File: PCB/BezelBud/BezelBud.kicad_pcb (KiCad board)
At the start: 4 copper layers, 64 parts, among them J1 USB_C_Receptacle_USB2.0_16P, J2 Conn_01x05_Pin, SW1 SW_SPDT, SW2 SW_SPDT, SW3 SW_SPDT, SW4 SW_SPDT, SW5 SW_SPDT, SW6 SW_SPDT, SW7 SW_SPDT, SW8 SW_SPDT, SW9 SW_SPDT, U1 STM32F072CBT6, U2 USBLC6-2SC6, U3 LP5907MFX-3.3, U4 LP5907MFX-3.3, U5 PCM1861DBT, Y1 Crystal_GND24

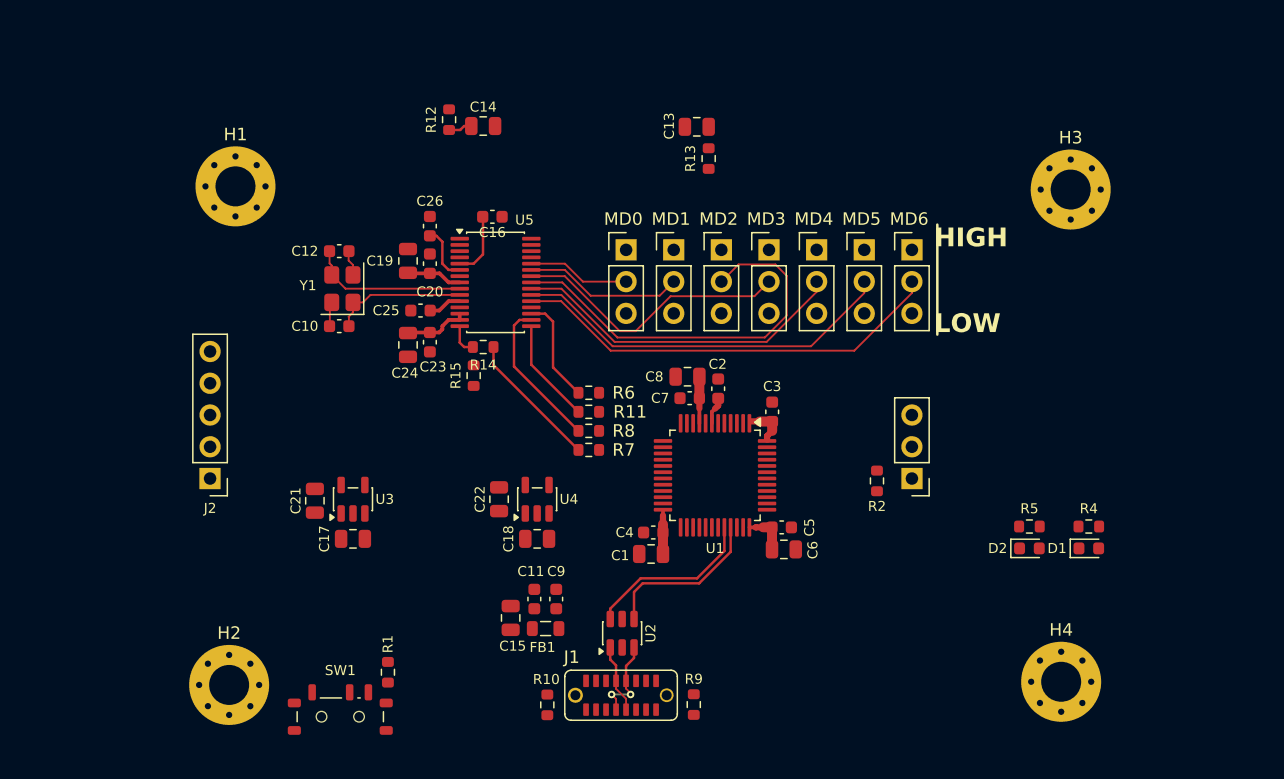
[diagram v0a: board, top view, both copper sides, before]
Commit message: small updates to schematic and layout for new stm32
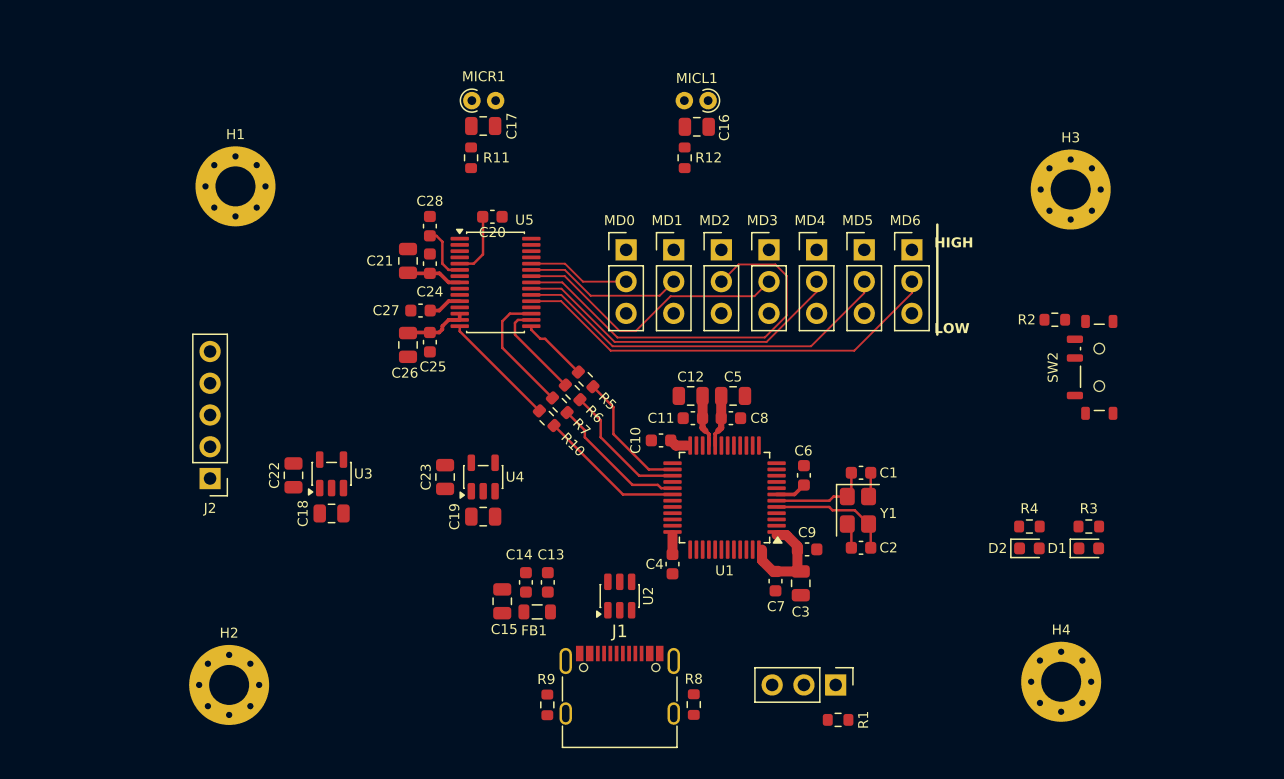
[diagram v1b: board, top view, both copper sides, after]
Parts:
- removed the C6 at (155.9, 82.1)
- removed R14, R15: 0R, Resistor_SMD:R_0603_1608Metric
- added C11: 0.1uF, Capacitor_SMD:C_0603_1608Metric, F.Cu at (148.6, 71.6)
- added C12: 1uF, Capacitor_SMD:C_0805_2012Metric, F.Cu at (148.4, 69.8)
- added C4: 0.1uF, Capacitor_SMD:C_0603_1608Metric, F.Cu at (147.0, 83.3)
- added MICL1: Microphone_Condenser, Resistor_THT:R_Axial_DIN0204_L3.6mm_D1.6mm_P1.90mm_Vertical, F.Cu at (149.8, 46.2)
- added MICR1: Microphone_Condenser, Resistor_THT:R_Axial_DIN0204_L3.6mm_D1.6mm_P1.90mm_Vertical, F.Cu at (130.9, 46.2)
- C5: value 0.1uF -> 1uF; footprint Capacitor_SMD:C_0603_1608Metric -> Capacitor_SMD:C_0805_2012Metric
- C7: value 10nF -> 0.1uF
- C8: value 1uF -> 10nF; footprint Capacitor_SMD:C_0805_2012Metric -> Capacitor_SMD:C_0603_1608Metric
- J1: footprint BezelBud:CONN RCPT Type-C 16POS SMD TC-005 -> Connector_USB:USB_C_Receptacle_G-Switch_GT-USB-7010ASV
- R3: renamed from R4; value 220 -> 1K
- R4: renamed from R5; value 220 -> 1K
- U1: value STM32F072CBT6 -> STM32G431CBT6
- moved SW2 66.8 mm to (181.1, 67.6), turned to 90 degrees
- moved R2 60.3 mm to (177.5, 63.8), turned to 0 degrees
- moved C2 48.0 mm to (162.0, 82.0), turned to 180 degrees
- moved Y1 44.9 mm to (161.8, 79.0), turned to -90 degrees
- moved C1 43.4 mm to (162.0, 76.0), turned to 0 degrees
- moved R1 19.4 mm to (160.2, 95.8), turned to 180 degrees
- moved SW1 17.6 mm to (160.0, 93.0), turned to -90 degrees
- moved C7 16.2 mm to (155.2, 84.7), turned to -90 degrees
- moved C3 12.2 mm to (157.2, 84.8), turned to -90 degrees
- moved C9 11.4 mm to (157.7, 82.1), turned to 0 degrees
- moved C5 11.2 mm to (151.8, 69.8)
- moved C6 9.75 mm to (157.5, 76.2)
- moved C10 7.39 mm to (146.1, 73.4)
- moved C8 4.80 mm to (151.6, 71.6), turned to 0 degrees
- moved C19 4.67 mm to (131.8, 79.5)
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- renumbered C10 to C1, C4 to C10, C9 to C13, C11 to C14, C13 to C16, C14 to C17, C17 to C18, C18 to C19, C12 to C2, C16 to C20, C19 to C21, C21 to C22, C22 to C23, C20 to C24, C23 to C25, C24 to C26, C25 to C27, C26 to C28, C1 to C3, C2 to C6, C3 to C9, R2 to R1, R7 to R10, R12 to R11, R13 to R12, R1 to R2, R11 to R5, R8 to R6, R6 to R7, R9 to R8, R10 to R9, SW2 to SW1, SW1 to SW2
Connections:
- C7 pad 1: +3.3VA -> +3.3V
- R10 pad 1: /I2S1_MCK -> /I2S2_MCK
- R10 pad 2: /I2S1_MCK_ST -> /I2S2_MCK_ST
- R5 pad 1: /I2S1_WS -> /I2S2_WS_ST
- R5 pad 2: /I2S1_WS_ST -> /I2S2_WS
- R6 pad 1: /I2S1_CK -> /I2S2_CK_ST
- R6 pad 2: /I2S1_CK_ST -> /I2S2_CK
- R7 pad 1: /I2S1_SD -> /I2S2_SD_ST
- R7 pad 2: /I2S1_SD_ST -> /I2S2_SD
- U1 pad 14: /I2S1_WS_ST -> unconnected-(U1-PA6-Pad14)
- U1 pad 15: /I2S1_CK_ST -> unconnected-(U1-PA7-Pad15)
- U1 pad 16: /I2S1_MCK_ST -> /LED_BLINK
- U1 pad 17: /I2S1_SD_ST -> /LED_LIVE
- U1 pad 18: unconnected-(U1-PB0-Pad18) -> /MUTE_SW
- U1 pad 19: unconnected-(U1-PB1-Pad19) -> GND
- U1 pad 20: unconnected-(U1-PB2-Pad20) -> +3.3VA
- U1 pad 21: unconnected-(U1-PB10-Pad21) -> +3.3VA
- U1 pad 26: /LED_BLINK -> /I2S2_WS_ST
- U1 pad 27: /LED_LIVE -> /I2S2_CK_ST
- U1 pad 28: /MUTE_SW -> unconnected-(U1-PB14-Pad28)
- U1 pad 29: unconnected-(U1-PA8-Pad29) -> /I2S2_SD_ST
- U1 pad 30: /INT -> /I2S2_MCK_ST
- U1 pad 31: unconnected-(U1-PA10-Pad31) -> /INT
- U1 pad 32: /USB_N -> unconnected-(U1-PA10-Pad32)
- U1 pad 33: /USB_P -> /USB_N
- U1 pad 34: /SWDIO -> /USB_P
- U1 pad 36: +3.3VA -> +3.3V
- U1 pad 37: /SWLCK -> /SWDIO
- U1 pad 38: unconnected-(U1-PA15-Pad38) -> /SWLCK
- U1 pad 44: /BOOT0 -> unconnected-(U1-PB7-Pad44)
- U1 pad 45: unconnected-(U1-PB8-Pad45) -> /BOOT0
- U1 pad 5: unconnected-(U1-PF0-Pad5) -> /PF0
- U1 pad 6: unconnected-(U1-PF1-Pad6) -> /PF1
- U1 pad 8: GND -> unconnected-(U1-PA0-Pad8)
- U1 pad 9: +3.3VA -> unconnected-(U1-PA1-Pad9)
- U5 pad 10: /PF1 -> unconnected-(U5-XI-Pad10)
- U5 pad 15: /SCKI -> /I2S2_MCK
- U5 pad 16: /I2S1_WS -> /I2S2_WS
- U5 pad 17: /I2S1_CK -> /I2S2_CK
- U5 pad 18: /I2S1_SD -> /I2S2_SD
- U5 pad 9: /PF0 -> unconnected-(U5-XO-Pad9)
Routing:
- net /USB_N: track 13.8 -> 0.00 mm
- net /USB_P: track 13.2 -> 0.00 mm
- net /I2S1_CK: track 12.1 -> 0.00 mm
- net /I2S2_MCK_ST: track 0.00 -> 11.8 mm
- net /I2S2_SD_ST: track 0.00 -> 11.3 mm
- net /I2S1_MCK: track 11.0 -> 0.00 mm
- net /I2S2_CK_ST: track 0.00 -> 10.7 mm
- net /I2S2_WS_ST: track 0.00 -> 10.4 mm
- net /I2S2_SD: track 0.00 -> 10.4 mm
- net /I2S2_MCK: track 0.00 -> 9.42 mm
- net /I2S1_SD: track 8.54 -> 0.00 mm
- net /I2S1_WS: track 8.41 -> 0.00 mm
- net /I2S2_CK: track 0.00 -> 8.05 mm
- net /USBC_P: track 6.95 -> 0.00 mm, vias 2 -> 0
- net /USBC_N: track 5.50 -> 0.00 mm
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
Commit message: updated pcb layout
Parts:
- added C18: 47uF, Capacitor_SMD:C_1206_3216Metric, F.Cu at (171.7, 92.3)
- added C20: 47uF, Capacitor_SMD:C_1206_3216Metric, F.Cu at (169.4, 92.3)
- added R13: 100R, Resistor_SMD:R_0805_2012Metric, F.Cu at (166.6, 91.0)
- moved J2 60.0 mm to (169.9, 75.2), turned to 0 degrees
- moved C26 47.7 mm to (176.3, 71.5), turned to 0 degrees
- moved C24 47.1 mm to (162.3, 87.6)
- moved H4 46.9 mm to (169.4, 46.6)
- moved H2 45.2 mm to (98.4, 49.7)
- moved C23 44.5 mm to (176.3, 78.0)
- moved U4 44.5 mm to (176.3, 74.8)
- moved SW3 44.0 mm to (112.0, 84.8)
- moved SW4 44.0 mm to (115.8, 84.8)
- moved SW5 44.0 mm to (127.3, 84.8)
- moved SW6 44.0 mm to (108.2, 84.8)
- moved SW7 44.0 mm to (119.6, 84.8)
- moved SW8 44.0 mm to (123.4, 84.8)
- moved SW9 44.0 mm to (131.1, 84.8)
- moved U3 40.9 mm to (158.9, 87.6), turned to 0 degrees
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- renumbered C18 to C19, C20 to C21, C21 to C22, C19 to C23, C22 to C24, C24 to C25, C23 to C26, C25 to C27, C26 to C28, C27 to C29, C28 to C30
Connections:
- C23 pad 1: +5V -> +5VFIL
- U4 pad 1: +5V -> +5VFIL
- U4 pad 3: +5V -> +5VFIL
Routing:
- net /MD6: track 34.9 -> 0.00 mm
- net /MD2: track 32.3 -> 0.00 mm
- net /MD5: track 31.0 -> 0.00 mm
- net /MD4: track 27.1 -> 0.00 mm
- net /MD3: track 22.5 -> 0.00 mm
- net /USB_N: track 0.00 -> 12.8 mm
- net /USB_P: track 0.00 -> 12.8 mm
- net /MD1: track 12.7 -> 0.00 mm
- net /I2S2_MCK_ST: track 11.8 -> 0.00 mm
- net /I2S2_SD_ST: track 11.3 -> 0.00 mm
- net /I2S2_CK_ST: track 10.7 -> 0.00 mm
- net /I2S2_WS_ST: track 10.4 -> 0.00 mm
- net /I2S2_MCK: track 9.42 -> 0.00 mm
- net /MD0: track 8.18 -> 0.00 mm
- net /VREF: track 4.54 -> 0.00 mm
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- removed copper zone on In1.Cu, net GND

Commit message: Updated PCB
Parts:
- added C31: 0.1uF, Capacitor_SMD:C_0603_1608Metric, F.Cu at (133.9, 94.2)
- added R14: 1M, Resistor_SMD:R_0603_1608Metric, F.Cu at (135.4, 94.3)
- moved H3 80.3 mm to (112.5, 93.2)
- moved H2 75.0 mm to (172.0, 64.0)
- moved SW2 65.1 mm to (125.5, 96.0), turned to 0 degrees
- moved R2 46.9 mm to (138.8, 84.8), turned to -90 degrees
- moved H4 46.7 mm to (172.0, 93.2)
- moved SW1 33.0 mm to (147.0, 84.9), turned to 90 degrees
- moved R4 28.2 mm to (159.8, 91.0)
- moved D2 28.1 mm to (159.8, 92.8)
- moved R3 28.0 mm to (164.7, 91.0)
- moved D1 27.9 mm to (164.8, 92.8)
- moved R1 25.3 mm to (154.5, 82.2), turned to 180 degrees
- moved H1 16.3 mm to (112.5, 64.0)
- moved R12 14.7 mm to (125.2, 64.4), turned to -90 degrees
- moved R8 12.4 mm to (148.8, 94.2)
- moved C18 10.1 mm to (173.2, 82.3), turned to 0 degrees
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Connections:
- net Net-(D1-A) renamed /R_A
- net Net-(D2-A) renamed /G_A
- J1 pad S1: GND -> /SHIELD
- U1 pad 16: /LED_BLINK -> unconnected-(U1-PB0-Pad16)
- U1 pad 17: /LED_LIVE -> unconnected-(U1-PB1-Pad17)
- U1 pad 18: /MUTE_SW -> unconnected-(U1-PB2-Pad18)
- U1 pad 41: unconnected-(U1-PB4-Pad41) -> /LED_BLINK
- U1 pad 42: unconnected-(U1-PB5-Pad42) -> /LED_LIVE
- U1 pad 43: unconnected-(U1-PB6-Pad43) -> /MUTE_SW
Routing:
- net +3.3VA: track 12.5 -> 93.0 mm
- net +3.3V: track 16.6 -> 73.6 mm, vias 0 -> 8
- net GND: track 4.01 -> 54.7 mm, vias 0 -> 199
- net /MUTE_SW: track 0.00 -> 37.6 mm, vias 0 -> 2
- net +5V: track 0.00 -> 34.7 mm
- net /LED_LIVE: track 0.00 -> 29.9 mm, vias 0 -> 2
- net /LED_BLINK: track 0.00 -> 29.0 mm, vias 0 -> 2
- net /MD0: track 0.00 -> 27.1 mm, vias 0 -> 1
- net /SWDIO: track 0.00 -> 24.9 mm, vias 0 -> 2
- net VCC: track 0.00 -> 24.1 mm
- net /SWLCK: track 0.00 -> 23.5 mm, vias 0 -> 2
- net /MD1: track 0.00 -> 22.9 mm, vias 0 -> 1
- net /SHIELD: track 0.00 -> 22.9 mm, vias 0 -> 1
- net /MD2: track 0.00 -> 22.8 mm, vias 0 -> 1
- net /INT: track 0.00 -> 20.3 mm, vias 0 -> 2
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- added copper zone on B.Cu, net +3.3V
- added copper zone on F.Cu, net +3.3V
- added copper zone on F.Cu, net GND
- added copper zone on In1.Cu, net GND
- added copper zone on In2.Cu, net GND
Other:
- board outline added: 70.1 x 39.6 mm
- board text added: "BEVEL"
- board text added: "BLINK"
- board text added: "DEBUG"
- board text added: "MUTE"
- board text added: "PRG"
- board text added: "RUN"
- board text added: "V1.0 - 02/14/2026"

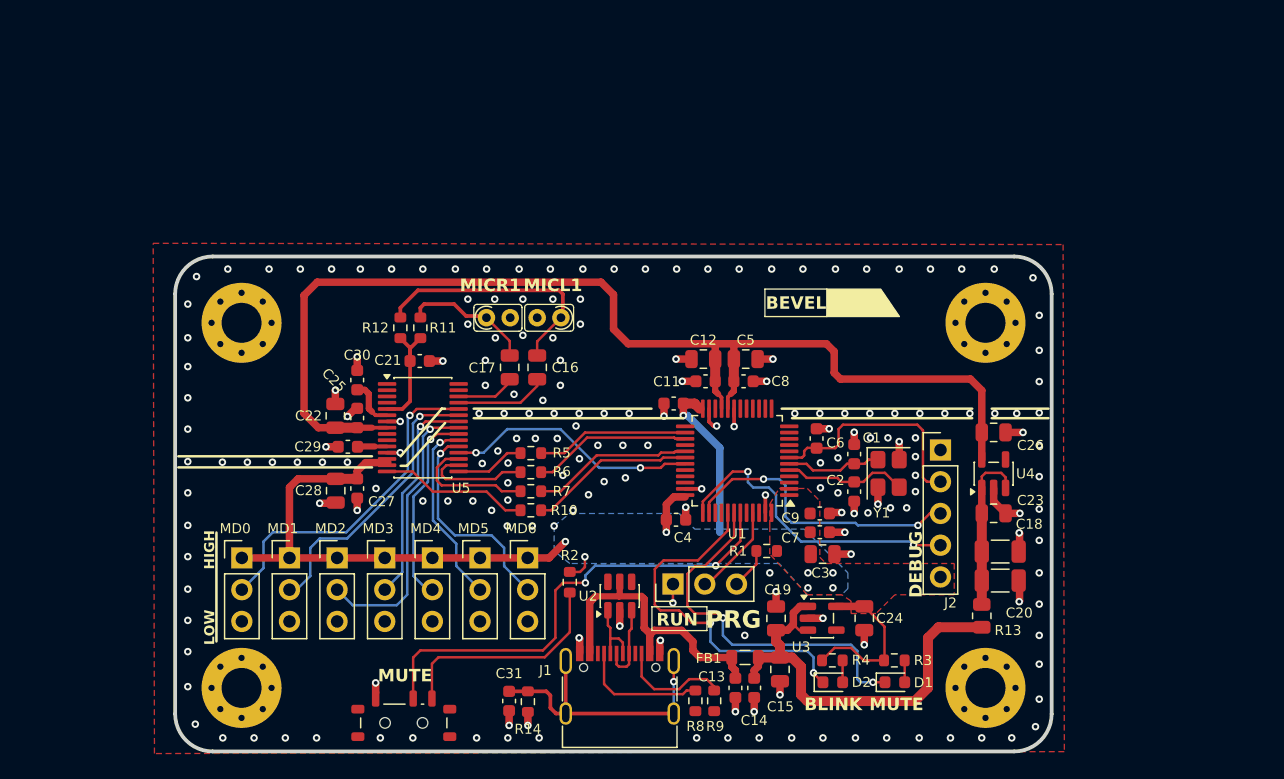
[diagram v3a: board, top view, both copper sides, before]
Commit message: Added bleed resistor and cap to shield <> GND con
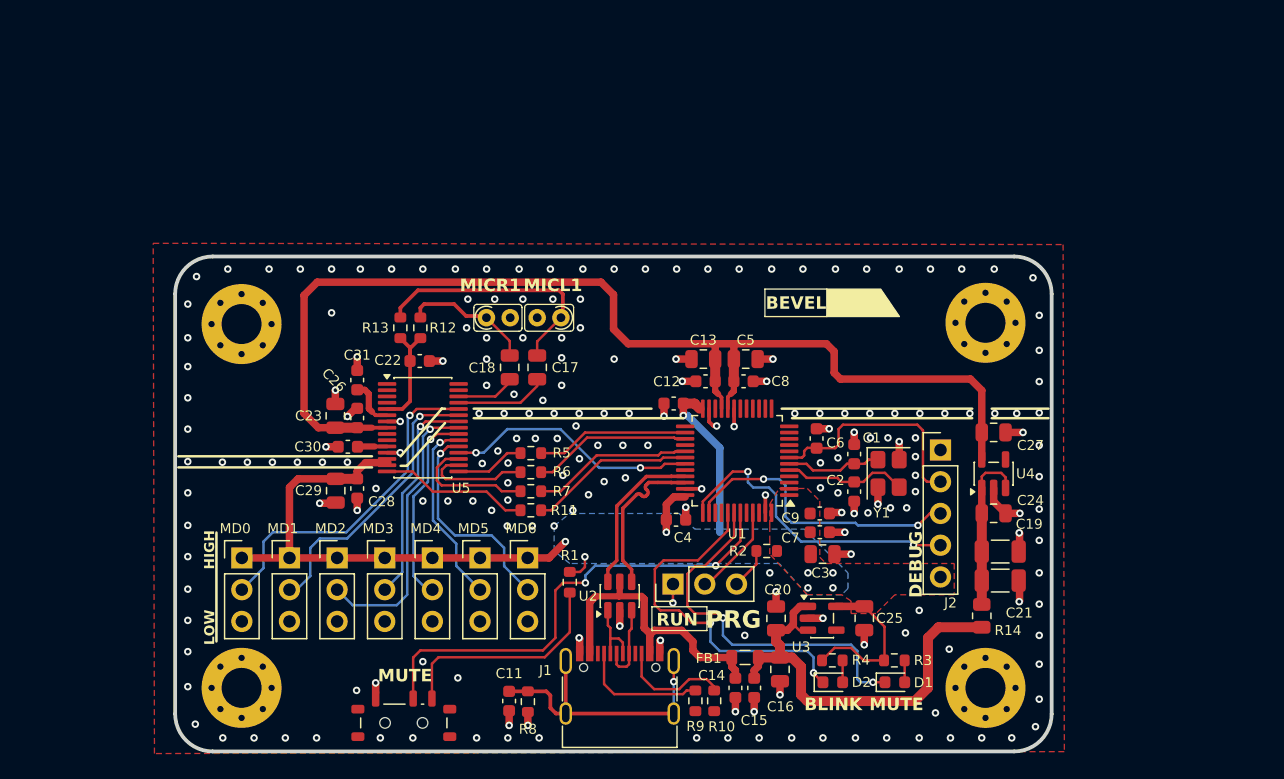
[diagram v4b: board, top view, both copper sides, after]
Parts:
- H1, H2, H3, H4: value MountingHole -> MountingHole_Pad
- moved H1 0.10 mm to (112.5, 64.1)
- renumbered C31 to C11, C11 to C12, C12 to C13, C13 to C14, C14 to C15, C15 to C16, C16 to C17, C17 to C18, C18 to C19, C19 to C20, C20 to C21, C21 to C22, C22 to C23, C23 to C24, C24 to C25, C25 to C26, C26 to C27, C27 to C28, C28 to C29, C29 to C30, C30 to C31, R2 to R1, R9 to R10, R10 to R11, R11 to R12, R12 to R13, R13 to R14, R1 to R2, R14 to R8, R8 to R9, SW2 to SW1, SW1 to SW2
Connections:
- net /INT renamed INT
- net /PF0 renamed PF0
- net /PF1 renamed PF1
- H1 pad 1: (no net) -> GND
- H2 pad 1: (no net) -> GND
- H3 pad 1: (no net) -> GND
- H4 pad 1: (no net) -> GND
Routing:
- net /USB_N: track 0.00 -> 12.8 mm
- net /USB_P: track 0.00 -> 12.8 mm
- net GND: vias 199 -> 208

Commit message: updated layout picture
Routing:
- net /USBC_P: track 6.42 -> 7.07 mm
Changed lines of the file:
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@@
-	)
-	(segment
-		(start 141.996 89.25)
-		(end 141.996 90.45)
-		(width 0.2)
-		(layer "F.Cu")
-		(net 22)
-	)
-	(segment
-		(start 141.996 88.402)
-		(end 141.996 89.25)
-		(width 0.2)
-		(layer "F.Cu")
-		(net 22)
-	)
-	(segment
-		(start 141.798 86.9895)
-		(end 141.798 88.204)
-		(width 0.2)
-		(layer "F.Cu")
-		(net 22)
-	)
-	(segment
-		(start 142.668 89.25)
-		(end 141.996 89.25)
-		(width 0.2)
-		(layer "F.Cu")
-		(net 22)
-	)
-	(segment
-		(start 141.798 88.204)
-		(end 141.996 88.402)
-		(width 0.2)
-		(layer "F.Cu")
-		(net 22)
 	)
 	(segment
 		(start 142.996 90.45)
-		(end 142.996 89.578)
-		(width 0.2)
-		(layer "F.Cu")
-		(net 22)
-	)
-	(segment
-		(start 142.996 89.578)
-		(end 142.668 89.25)
-		(width 0.2)
+		(end 143.006 90.44)
+		(width 0.28)
+		(layer "F.Cu")
+		(net 22)
+	)
+	(segment
+		(start 142.8 89.3)
+		(end 141.996 89.3)
+		(width 0.28)
+		(layer "F.Cu")
+		(net 22)
+	)
+	(segment
+		(start 141.996 88.704)
+		(end 142 88.7)
+		(width 0.3)
+		(layer "F.Cu")
+		(net 22)
+	)
+	(segment
+		(start 141.996 89.3)
+		(end 141.996 88.704)
+		(width 0.3)
+		(layer "F.Cu")
+		(net 22)
+	)
+	(segment
+		(start 142.996 89.496)
+		(end 142.8 89.3)
+		(width 0.28)
+		(layer "F.Cu")
+		(net 22)
+	)
+	(segment
+		(start 142.996 90.45)
+		(end 142.996 89.496)
+		(width 0.28)
+		(layer "F.Cu")
+		(net 22)
+	)
+	(segment
+		(start 141.996 90.45)
+		(end 141.996 89.3)
+		(width 0.3)
+		(layer "F.Cu")
+		(net 22)
+	)
+	(segment
+		(start 141.798 88.498)
+		(end 141.798 86.9895)
+		(width 0.3)
+		(layer "F.Cu")
+		(net 22)
+	)
+	(segment
+		(start 142 88.7)
+		(end 141.798 88.498)
+		(width 0.3)
+		(layer "F.Cu")
+		(net 22)
+	)
+	(segment
+		(start 143.006 90.44)
+		(end 143.006 90.277508)
+		(width 0.28)
 		(layer "F.Cu")
 		(net 22)
@@
 	)
 	(segment
+		(start 143.698 88.502)
+		(end 143.698 86.9895)
+		(width 0.28)
+		(layer "F.Cu")
+		(net 25)
+	)
+	(segment
+		(start 143.496 88.704)
+		(end 143.698 88.502)
+		(width 0.28)
+		(layer "F.Cu")
+		(net 25)
+	)
+	(segment
+		(start 143.496 91.504)
+		(end 143.496 90.45)
+		(width 0.3)
+		(layer "F.Cu")
+		(net 25)
+	)
+	(segment
 		(start 143.496 90.45)
-		(end 143.496 91.301241)
-		(width 0.2)
-		(layer "F.Cu")
-		(net 25)
-	)
-	(segment
-		(start 142.496 91.322)
-		(end 142.496 90.45)
-		(width 0.2)
-		(layer "F.Cu")
-		(net 25)
-	)
-	(segment
-		(start 143.698 88.458)
-		(end 143.698 86.9895)
-		(width 0.2)
-		(layer "F.Cu")
-		(net 25)
-	)
-	(segment
-		(start 143.297241 91.5)
-		(end 142.674 91.5)
-		(width 0.2)
-		(layer "F.Cu")
-		(net 25)
-	)
-	(segment
-		(start 142.674 91.5)
-		(end 142.496 91.322)
-		(width 0.2)
+		(end 143.496 88.704)
+		(width 0.28)
+		(layer "F.Cu")
+		(net 25)
+	)
+	(segment
+		(start 142.8 91.8)
+		(end 143.2 91.8)
+		(width 0.3)
+		(layer "F.Cu")
+		(net 25)
+	)
+	(segment
+		(start 142.496 91.496)
+		(end 142.8 91.8)
+		(width 0.3)
 		(layer "F.Cu")
 		(net 25)
@@
 	(segment
 		(start 143.496 90.45)
-		(end 143.496 88.66)
-		(width 0.2)
-		(layer "F.Cu")
-		(net 25)
-	)
-	(segment
-		(start 143.496 88.66)
-		(end 143.698 88.458)
-		(width 0.2)
-		(layer "F.Cu")
-		(net 25)
-	)
-	(segment
-		(start 143.496 91.301241)
-		(end 143.297241 91.5)
-		(width 0.2)
-		(layer "F.Cu")
-		(net 25)
+		(end 143.486 90.44)
+		(width 0.28)
+		(layer "F.Cu")
+		(net 25)
+	)
+	(segment
+		(start 143.486 90.44)
+		(end 143.486 90.277508)
+		(width 0.28)
+		(layer "F.Cu")
+		(net 25)
+	)
+	(segment
+		(start 142.496 90.45)
+		(end 142.496 91.496)
+		(width 0.3)
+		(layer "F.Cu")
+		(net 25)
+	)
+	(segment
+		(start 143.2 91.8)
+		(end 143.496 91.504)
+		(width 0.3)
+		(layer "F.Cu")
+		(net 25)
